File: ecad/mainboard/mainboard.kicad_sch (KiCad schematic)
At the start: 50 parts, among them J1 TYPE-C-31-M-12, J2 SWD, SW3 SW_Push, SW4 SW_Push, U1 NCP1117ST33T3G, U2 USBLC6-2SC6, U2 W25Q128JVS, U3 RP2040, Y1 ABM8-272-T3

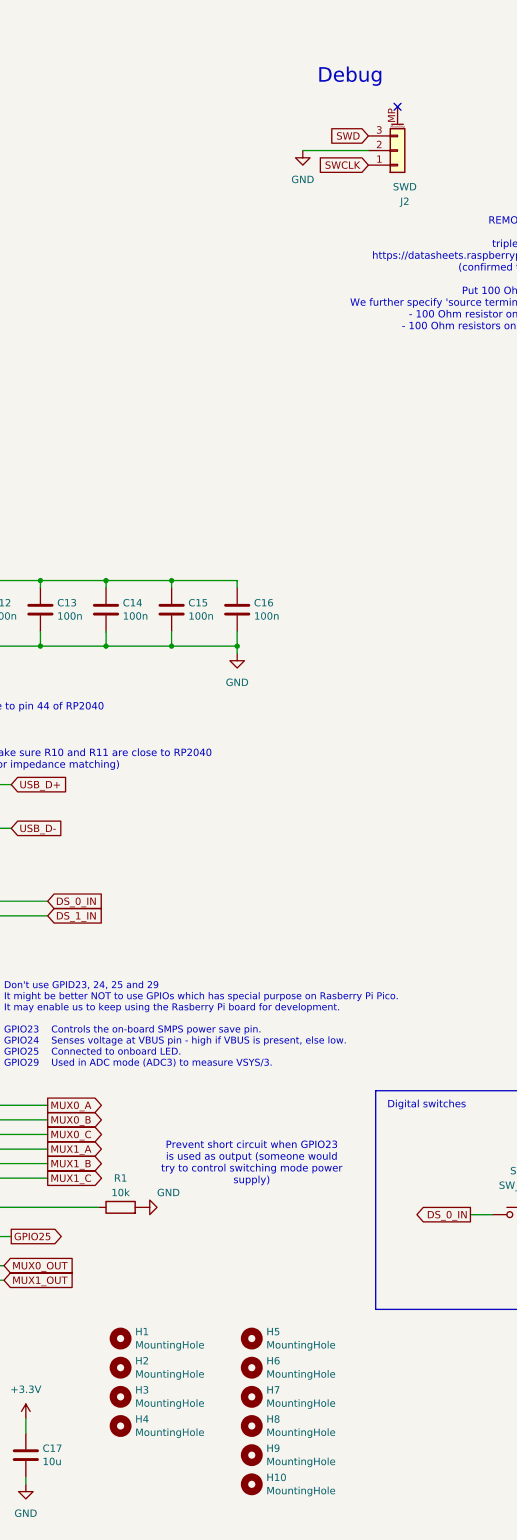
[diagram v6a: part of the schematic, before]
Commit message: Place all buttons
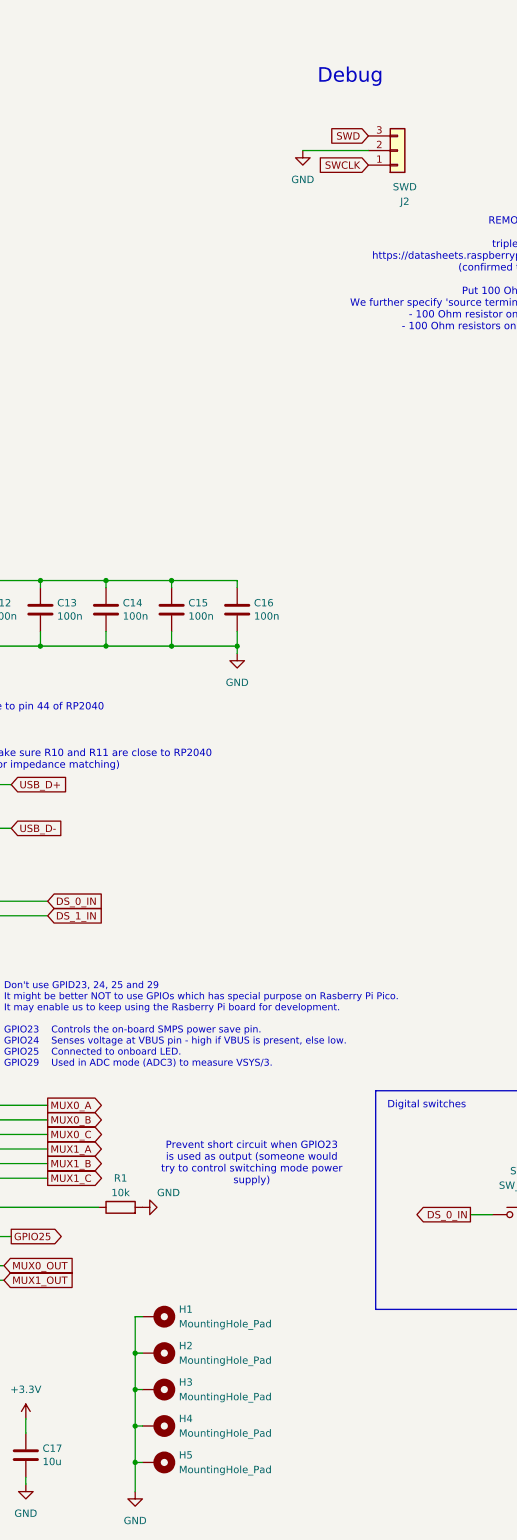
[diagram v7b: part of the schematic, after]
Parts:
- removed H1, H10, H2, H3, H4, H5, H6, H7, H8, H9: MountingHole, MountingHole:MountingHole_2.7mm_M2.5, symbol Mechanical:MountingHole
- added H1, H2, H3, H4, H5: MountingHole_Pad, MountingHole:MountingHole_2.7mm_M2.5_Pad_Via, symbol Mechanical:MountingHole_Pad
- J2: symbol Connector_Generic_MountingPin:Conn_01x03_MountingPin -> Connector_Generic:Conn_01x03
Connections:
- net GND: now also H1.1, H2.1, H3.1, H4.1, H5.1
- no-connect marks 4 -> 3

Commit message: rev2 board
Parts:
- D1: JCSC C2297 -> (none); LCSC (none) -> C2297
- H1, H2, H3, H4, H5: footprint MountingHole:MountingHole_2.7mm_M2.5_Pad_Via -> MountingHole:MountingHole_3.7mm_Pad_Via
- J1: JCSC C165948 -> (none); LCSC (none) -> C165948
- J2: JCSC C160403 -> (none); LCSC (none) -> C160403
- SW3, SW4: JLCPCB C5156480 -> (none); LCSC (none) -> C5156480
- U1: JCSC C26537 -> (none); LCSC (none) -> C26537
- U2: JCSC C2827654 -> (none); LCSC (none) -> C2827654
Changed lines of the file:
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@@
 			)
 		)
-		(property "Footprint" "MountingHole:MountingHole_2.7mm_M2.5_Pad_Via"
+		(property "Footprint" "MountingHole:MountingHole_3.7mm_Pad_Via"
 			(at 262.89 270.51 0)
 			(effects
@@
 			)
 		)
-		(property "Footprint" "MountingHole:MountingHole_2.7mm_M2.5_Pad_Via"
+		(property "Footprint" "MountingHole:MountingHole_3.7mm_Pad_Via"
 			(at 262.89 264.16 0)
 			(effects
@@
 			)
 		)
-		(property "JCSC" "C160403"
+		(property "LCSC" "C160403"
 			(at 304.8 41.91 0)
 			(effects
@@
 			)
 		)
-		(property "JLCPCB" "C5156480"
+		(property "LCSC" "C5156480"
 			(at 384.81 227.33 0)
 			(effects
@@
 			)
 		)
-		(property "JCSC" "C2827654"
+		(property "LCSC" "C2827654"
 			(at 81.28 49.53 0)
 			(effects
@@
 			)
 		)
-		(property "JLCPCB" "C5156480"
+		(property "LCSC" "C5156480"
 			(at 326.39 227.33 0)
 			(effects
@@
 			)
 		)
-		(property "JCSC" "C2297"
+		(property "LCSC" "C2297"
 			(at 360.68 187.96 0)
 			(effects
@@
 			)
 		)
-		(property "Footprint" "MountingHole:MountingHole_2.7mm_M2.5_Pad_Via"
+		(property "Footprint" "MountingHole:MountingHole_3.7mm_Pad_Via"
 			(at 262.89 245.11 0)
 			(effects
@@
 			)
 		)
-		(property "JCSC" "C165948"
+		(property "LCSC" "C165948"
 			(at 34.29 49.53 0)
 			(effects
@@
 			)
 		)
-		(property "Footprint" "MountingHole:MountingHole_2.7mm_M2.5_Pad_Via"
+		(property "Footprint" "MountingHole:MountingHole_3.7mm_Pad_Via"
 			(at 262.89 257.81 0)
 			(effects
@@
 			)
 		)
-		(property "Footprint" "MountingHole:MountingHole_2.7mm_M2.5_Pad_Via"
+		(property "Footprint" "MountingHole:MountingHole_3.7mm_Pad_Via"
 			(at 262.89 251.46 0)
 			(effects
@@
 			)
 		)
-		(property "JCSC" "C26537"
+		(property "LCSC" "C26537"
 			(at 168.91 36.83 0)
 			(effects
